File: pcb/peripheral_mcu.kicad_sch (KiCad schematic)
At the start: 4 parts, among them U4 STM32C071RBTx

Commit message: tons of work on rf and mcu
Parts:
- removed C27: 4.7uF, symbol Device:C
- removed U4: STM32C071RBTx, Package_QFP:LQFP-64_10x10mm_P0.5mm, symbol MCU_ST_STM32C0:STM32C071RBTx
- added C27: 22uF, symbol Device:C_Small
- added C30, C31, C32, C33, C34, C35: 100nF, symbol Device:C
- added C36: 1uF, symbol Device:C
- added IC1: STM32C552MET6, QFP50P1400X1400X160-80N, symbol STM32C552MET6:STM32C552MET6
- added IC2: S25FL256LAGNFI010, SON127P800X600X80-9N-D, symbol S25FL256LAGNFI010:S25FL256LAGNFI010
- added R11: 10k, symbol Device:R
- C29: value 100nF -> 4.7uF
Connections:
- net +3.3V: now also C30.1, C31.1, C32.1, C33.1, C34.1, C35.1, C36.1, IC1.16 (VREF+), IC1.23 (VDD_2), IC1.40 (VDD_3), IC1.60 (VDD_4), IC1.7 (VDD_1), IC1.80 (VDD_5), IC2.8 (VCC), R11.1
- net GND: now also C27.2, C30.2, C31.2, C32.2, C33.2, C34.2, C35.2, C36.2, IC1.15 (VREF-), IC1.22 (VSS_2), IC1.39 (VSS_3), IC1.59 (VSS_4), IC1.6 (VSS_1), IC1.79 (VSS_5), IC2.4 (VSS), IC2.9 (EP)
- new net: C27.1, IC1.38 (VCAP)
- new net flash_clk: IC1.42 (PB13), IC2.6 (SCK)
- new net flash_cs: IC2.1 (CS#), R11.2
- new net flash_miso: IC1.43 (PB14), IC2.2 (SO/IO1)
- new net flash_mosi: IC1.44 (PB15), IC2.5 (SI/IO0)
- new net flash_rst: IC2.7 (IO3/RESET#)
- new net flash_wp: IC2.3 (WP#/IO2)
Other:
- note added: "WHYY IS THE SYMBOL SO BADDDDD MOUSER YOU HAVE FAILED MEEEE"
- note added: "flash"
- note added: "forgive me for this sin against schematic practices but the symbol made me"
- note added: "vdd decoupling"
- note added: "vref+ decoupling"

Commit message: added missing files, rf stuff done I think (hope)
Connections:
- net mcu->ppu_sck: now reaches IC1.25 (PA5)
- net mcu->ppu_mosi: now reaches IC1.26 (PA6)
- net mcu->ppu_miso: now reaches IC1.27 (PA7)
- net lr_nrst: now reaches IC1.29 (PC5)
- net lr_miso: now reaches IC1.30 (PB0)
- net lr_sck: now reaches IC1.31 (PB1)
- net lr_mosi: now reaches IC1.32 (PB2)
- net lr_nss: now reaches IC1.33 (PE7)
- net lr_busy: now reaches IC1.34 (PE8)
- net lr_irq1: now reaches IC1.35 (PE9)
- net lr_irq2: now reaches IC1.36 (PE10)

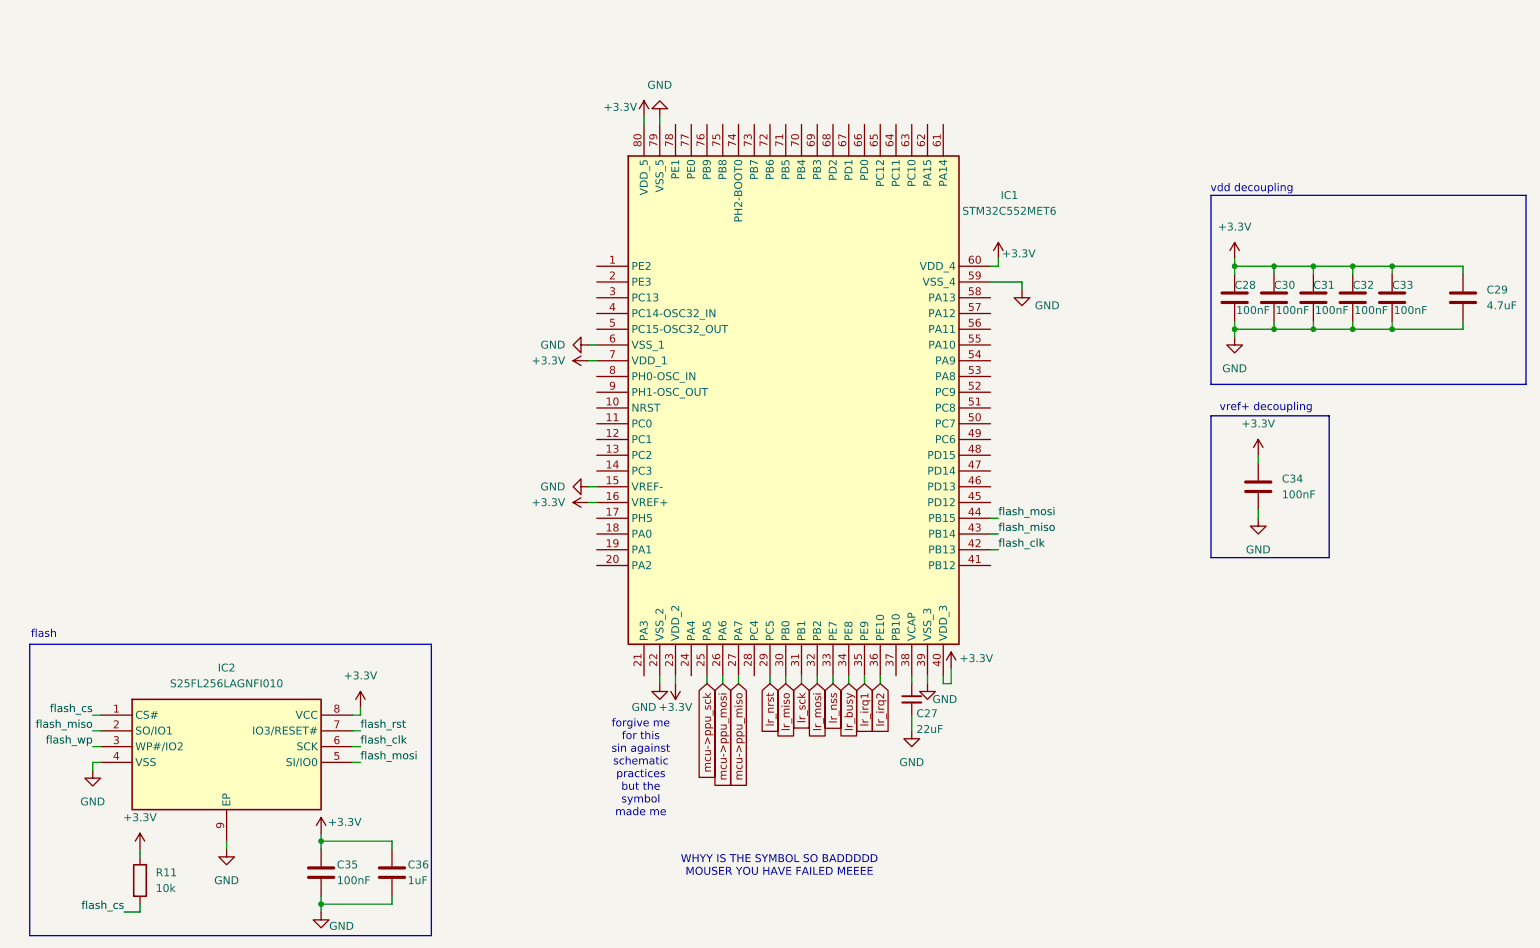
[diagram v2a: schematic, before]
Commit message: got fets figured out (finally), can integrated, a 5v regulator, sensors added - overall great progress!
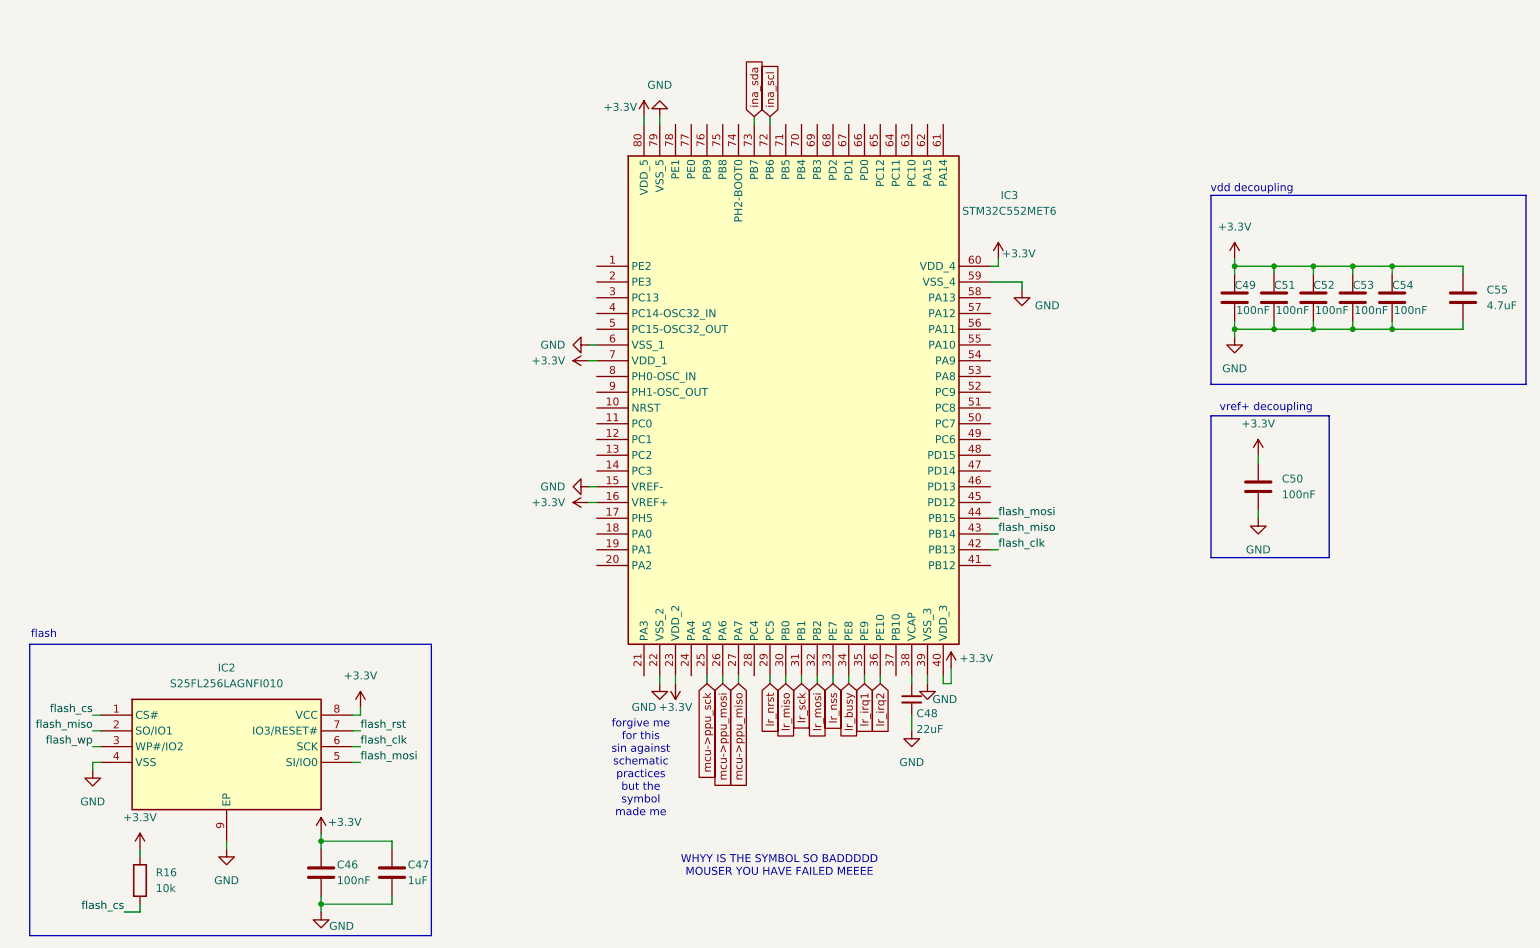
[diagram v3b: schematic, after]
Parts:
- renumbered C35 to C46, C36 to C47, C27 to C48, C28 to C49, C34 to C50, C30 to C51, C31 to C52, C32 to C53, C33 to C54, C29 to C55, IC1 to IC3, R11 to R16
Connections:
- net ina_scl: now reaches IC3.72 (PB6)
- net ina_sda: now reaches IC3.73 (PB7)

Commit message: pretty much everything on schem done, though need to add circuit protection stuff and break out remaining pins
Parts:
- added C39, C41: 8pF, symbol Device:C_Small
- added C40, C42: 17pF, symbol Device:C_Small
- added C43: 100nF, symbol Device:C
- added D6: STATUS, symbol Device:LED
- added J6: Conn_02x04_Top_Bottom, symbol Connector_Generic:Conn_02x04_Top_Bottom
- added JP3: BOOT, TestPoint:TestPoint_2Pads_Pitch2.54mm_Drill0.8mm, symbol Jumper:Jumper_2_Open
- added JP4: RST, TestPoint:TestPoint_2Pads_Pitch2.54mm_Drill0.8mm, symbol Jumper:Jumper_2_Open
- added R23, R24, R25: 10k, symbol Device:R
- added R26, R27: 1k, symbol Device:R_Small
- added R28: 120, symbol Device:R
- added Y3: 24mHz 8pf, symbol Device:Crystal_GND24
- added Y4: 32.768kHz 12.5pF, symbol Device:Crystal
- renumbered C46 to C44, C47 to C45, C48 to C46, C49 to C47, C50 to C48, C51 to C49, C52 to C50, C53 to C51, C54 to C52, C55 to C53, R16 to R22
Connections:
- net +3.3V: now also J6.8 (Pin_8), JP3.1 (A), R24.1
- net GND: now also C39.1, C40.1, C41.2, C42.2, C43.2, J6.2 (Pin_2), J6.4 (Pin_4), JP4.1 (A), R23.2, R28.1, Y3.2 (G), Y3.4 (G)
- net rst: now reaches IC3.10 (NRST)
- net rst: now also C43.1, J6.3 (Pin_3), JP4.2 (B), R24.2
- net cont_test: now reaches IC3.18 (PA0)
- net ppu_usart2_tx: now reaches IC3.20 (PA2)
- net ppu_usart2_rx: now reaches IC3.21 (PA3)
- net ppu_i2c2_scl: now reaches IC3.37 (PB10)
- net lse_0: now reaches IC3.4 (PC14-OSC32_IN)
- net lse_0: now also C40.2, Y4.1
- net ppu_i2c2_sda: now reaches IC3.41 (PB12)
- net camera_enable: now reaches IC3.46 (PD13)
- net c6_fire: now reaches IC3.47 (PD14)
- net c5_fire: now reaches IC3.48 (PD15)
- net c4_fire: now reaches IC3.49 (PC6)
- net at IC3.5 (PC15-OSC32_OUT): now also R26.1
- net c3_fire: now reaches IC3.50 (PC7)
- net c2_fire: now reaches IC3.51 (PC8)
- net c1_fire: now reaches IC3.52 (PC9)
- net arm: now reaches IC3.53 (PA8)
- net ppu_usart1_tx: now reaches IC3.54 (PA9)
- net ppu_usart1_rx: now reaches IC3.55 (PA10)
- net usb2_d-: now reaches IC3.56 (PA11)
- net usb2_d+: now reaches IC3.57 (PA12)
- net swdio: now reaches IC3.58 (PA13)
- net swdio: now also J6.5 (Pin_5)
- net swclk: now reaches IC3.61 (PA14)
- net swclk: now also J6.6 (Pin_6)
- net swo: now reaches IC3.69 (PB3)
- net swo: now also J6.1 (Pin_1)
- net boot: now reaches IC3.74 (PH2-BOOT0)
- net boot: now also J6.7 (Pin_7), R25.2
- net at IC3.78 (PE1): now also D6.2 (A)
- net hse_0: now reaches IC3.8 (PH0-OSC_IN)
- net hse_0: now also C39.2, Y3.1
- net at IC3.9 (PH1-OSC_OUT): now also R27.2
- new net: JP3.2 (B), R23.1, R25.1
- new net: D6.1 (K), R28.2
- new net hse_1: C41.1, R27.1, Y3.3
- new net lse_1: C42.1, R26.2, Y4.2
- no-connect marks 0 -> 2
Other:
- note added: "bootsel"
- note added: "debug"
- note added: "hse"
- note added: "lse"
- note added: "reset"

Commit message: yay schematic pretty much good, though I'm going to have to redo some work to split it into multiple kicad projects so I can have multiple separate boards
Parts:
- C39, C40, C41, C42, C43, C44, C47, C48, C49, C50, C51, C52: footprint (none) -> Capacitor_SMD:C_0402_1005Metric
- C45, C53: footprint (none) -> Capacitor_SMD:C_0603_1608Metric
- C46: value 22uF -> 2.2uF; footprint (none) -> Capacitor_SMD:C_0603_1608Metric
- IC2: footprint SON127P800X600X80-9N-D -> S25FL256LAGNFI010:SON127P800X600X80-9N-D
- IC3: footprint QFP50P1400X1400X160-80N -> STM32C552ME:QFP50P1400X1400X160-80N
- R22, R23, R24, R25, R26, R27: footprint (none) -> Resistor_SMD:R_0402_1005Metric
- R28: footprint (none) -> Resistor_SMD:R_0603_1608Metric
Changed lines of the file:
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@@
 			)
 		)
-		(property "Footprint" ""
+		(property "Footprint" "Resistor_SMD:R_0402_1005Metric"
 			(at 63.5 90.678 90)
 			(effects
@@
 			)
 		)
-		(property "Value" "22uF"
+		(property "Value" "2.2uF"
 			(at 155.702 154.686 0)
 			(effects
@@
 			)
 		)
-		(property "Footprint" ""
+		(property "Footprint" "Capacitor_SMD:C_0603_1608Metric"
 			(at 154.94 149.86 0)
 			(effects
@@
 			)
 		)
-		(property "Footprint" ""
+		(property "Footprint" "Capacitor_SMD:C_0402_1005Metric"
 			(at 227.0252 88.9 0)
 			(effects
@@
 			)
 		)
-		(property "Footprint" ""
+		(property "Footprint" "Capacitor_SMD:C_0603_1608Metric"
 			(at 72.0852 181.61 0)
 			(effects
@@
 			)
 		)
-		(property "Footprint" ""
+		(property "Footprint" "Capacitor_SMD:C_0402_1005Metric"
 			(at 214.3252 88.9 0)
 			(effects
@@
 			)
 		)
-		(property "Footprint" ""
+		(property "Footprint" "Resistor_SMD:R_0402_1005Metric"
 			(at 56.642 93.98 90)
 			(effects
@@
 			)
 		)
-		(property "Footprint" ""
+		(property "Footprint" "Capacitor_SMD:C_0402_1005Metric"
 			(at 22.86 67.31 0)
 			(effects
@@
 			)
 		)
-		(property "Footprint" ""
+		(property "Footprint" "Capacitor_SMD:C_0402_1005Metric"
 			(at 207.9752 88.9 0)
 			(effects
@@
 			)
 		)
-		(property "Footprint" ""
+		(property "Footprint" "Capacitor_SMD:C_0402_1005Metric"
 			(at 233.3752 88.9 0)
 			(effects
@@
 			)
 		)
-		(property "Footprint" ""
+		(property "Footprint" "Capacitor_SMD:C_0402_1005Metric"
 			(at 211.7852 119.38 0)
 			(effects
@@
 			)
 		)
-		(property "Footprint" ""
+		(property "Footprint" "Resistor_SMD:R_0402_1005Metric"
 			(at 57.912 62.23 90)
 			(effects
@@
 			)
 		)
-		(property "Footprint" ""
+		(property "Footprint" "Capacitor_SMD:C_0402_1005Metric"
 			(at 49.53 72.0852 0)
 			(effects
@@
 			)
 		)
-		(property "Footprint" ""
+		(property "Footprint" "Capacitor_SMD:C_0402_1005Metric"
 			(at 22.86 93.98 0)
 			(effects
@@
 			)
 		)
-		(property "Footprint" ""
+		(property "Footprint" "Capacitor_SMD:C_0402_1005Metric"
 			(at 220.6752 88.9 0)
 			(effects
@@
 			)
 		)
-		(property "Footprint" ""
+		(property "Footprint" "Resistor_SMD:R_0402_1005Metric"
 			(at 96.52 90.17 0)
 			(effects
@@
 			)
 		)
-		(property "Footprint" ""
+		(property "Footprint" "Capacitor_SMD:C_0402_1005Metric"
 			(at 33.02 93.98 0)
 			(effects
@@
 			)
 		)
-		(property "Footprint" "SON127P800X600X80-9N-D"
+		(property "Footprint" "S25FL256LAGNFI010:SON127P800X600X80-9N-D"
 			(at 60.96 247.32 0)
 			(effects
@@
 			)
 		)
-		(property "Footprint" ""
+		(property "Footprint" "Resistor_SMD:R_0402_1005Metric"
 			(at 100.33 100.33 0)
 			(effects
@@
 			)
 		)
-		(property "Footprint" ""
+		(property "Footprint" "Capacitor_SMD:C_0603_1608Metric"
 			(at 244.8052 88.9 0)
 			(effects
@@
 			)
 		)
-		(property "Footprint" ""
+		(property "Footprint" "Capacitor_SMD:C_0402_1005Metric"
 			(at 33.02 67.31 0)
 			(effects
@@
 			)
 		)
-		(property "Footprint" ""
+		(property "Footprint" "Capacitor_SMD:C_0402_1005Metric"
 			(at 60.6552 181.61 0)
 			(effects
@@
 			)
 		)
-		(property "Footprint" ""
+		(property "Footprint" "Resistor_SMD:R_0402_1005Metric"
 			(at 28.702 179.07 90)
 			(effects
@@
 			)
 		)
-		(property "Footprint" ""
+		(property "Footprint" "Resistor_SMD:R_0603_1608Metric"
 			(at 102.87 47.498 90)
 			(effects
@@
 			)
 		)
-		(property "Footprint" "QFP50P1400X1400X160-80N"
+		(property "Footprint" "STM32C552ME:QFP50P1400X1400X160-80N"
 			(at 163.83 159.69 0)
 			(effects
